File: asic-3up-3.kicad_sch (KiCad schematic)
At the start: 80 parts, among them J10 Conn_01x01, J11 Conn_01x01, J21 Conn_01x01, U4 SN74AVC4T774, U5 25MHz, U66 MCP1824T-1202E/OT, U67 MCP1824T-1202E/OT, U68 MCP1824T-1202E/OT, U69 MCP1824T-0802E, U70 MCP1824T-0802E, U71 MCP1824T-0802E, U72 BM1362AC_MODE1, U73 BM1362AC_MODE0, U74 BM1362AC_MODE1

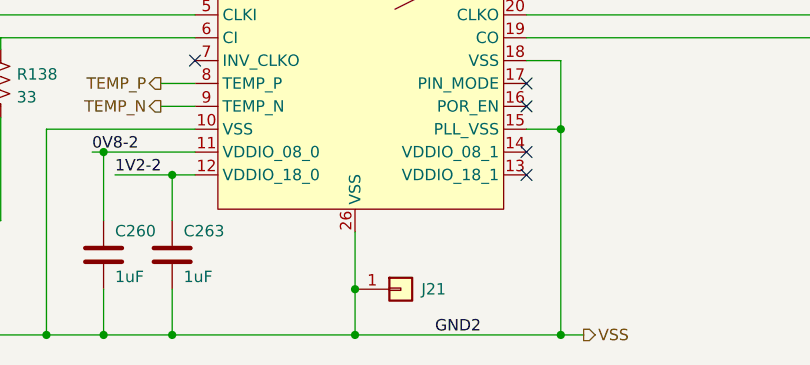
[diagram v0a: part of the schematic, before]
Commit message: remove all power pads, replace with planes, including on back layer. regenerate BOM
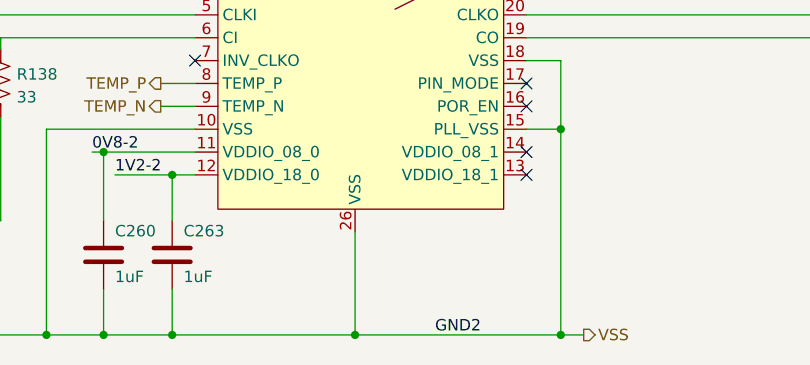
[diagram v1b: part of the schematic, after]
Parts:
- removed J21: Conn_01x01, emberone:14x9_powertab_L, symbol Connector_Generic:Conn_01x01
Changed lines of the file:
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@@
 	)
 	(junction
-		(at 260.35 250.19)
-		(diameter 0)
-		(color 0 0 0 0)
-	)
-	(junction
 		(at 73.66 57.15)
 		(diameter 0)
@@
 	(wire
 		(pts
-			(xy 260.35 243.84) (xy 260.35 250.19)
+			(xy 260.35 243.84) (xy 260.35 255.27)
 		)
 		(stroke
@@
 	(wire
 		(pts
-			(xy 260.35 250.19) (xy 260.35 255.27)
-		)
-		(stroke
-			(width 0)
-			(type default)
-		)
-	)
-	(wire
-		(pts
 			(xy 297.18 203.2) (xy 297.18 209.55)
 		)
@@
 					(unit 1)
 				)
-			)
-		)
-	)
-	(symbol
-		(lib_id "Connector_Generic:Conn_01x01")
-		(at 265.43 250.19 0)
-		(unit 1)
-		(exclude_from_sim no)
-		(in_bom yes)
-		(on_board yes)
-		(dnp no)
-		(property "Reference" "J21"
-			(at 267.716 250.19 0)
-			(effects
-				(font
-					(size 1.27 1.27)
-				)
-				(justify left)
-			)
-		)
-		(property "Value" "Conn_01x01"
-			(at 267.97 251.4599 0)
-			(effects
-				(font
-					(size 1.27 1.27)
-				)
-				(justify left)
-				(hide yes)
-			)
-		)
-		(property "Footprint" "emberone:14x9_powertab_L"
-			(at 265.43 250.19 0)
-			(effects
-				(font
-					(size 1.27 1.27)
-				)
-				(hide yes)
-			)
-		)
-		(property "Datasheet" "~"
-			(at 265.43 250.19 0)
-			(effects
-				(font
-					(size 1.27 1.27)
-				)
-				(hide yes)
-			)
-		)
-		(property "Description" "powertab"
-			(at 265.43 250.19 0)
-			(effects
-				(font
-					(size 1.27 1.27)
-				)
-				(hide yes)
-			)
-		)
-		(pin "1"
-		)
-		(instances
-			(project "emberone"
-				(path "/b036224c-4cdf-48cc-81df-19bc5283ebd2/75fd7cab-4b1e-4fa4-8631-02e52962bbf8"
-					(reference "J21")
-					(unit 1)
-				)
